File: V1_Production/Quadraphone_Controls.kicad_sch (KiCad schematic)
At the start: 20 parts, among them J1 Conn_01x10_Female, J10 Pitch_In, J11 Mix_Out, J12 Conn_02x04_Top_Bottom, J13 Conn_01x04_Male, J14 Conn_01x01_Male, J2 Conn_01x10_Female, J3 Conn_01x10_Female, J4 Conn_01x10_Female, J5 PWM_CV, J6 LFO_IN, J7 PWM_CV_In, J8 Synch_Signal_In, J9 Freq_Mod_In, SW1 Synch_Type, SW2 Output_Type

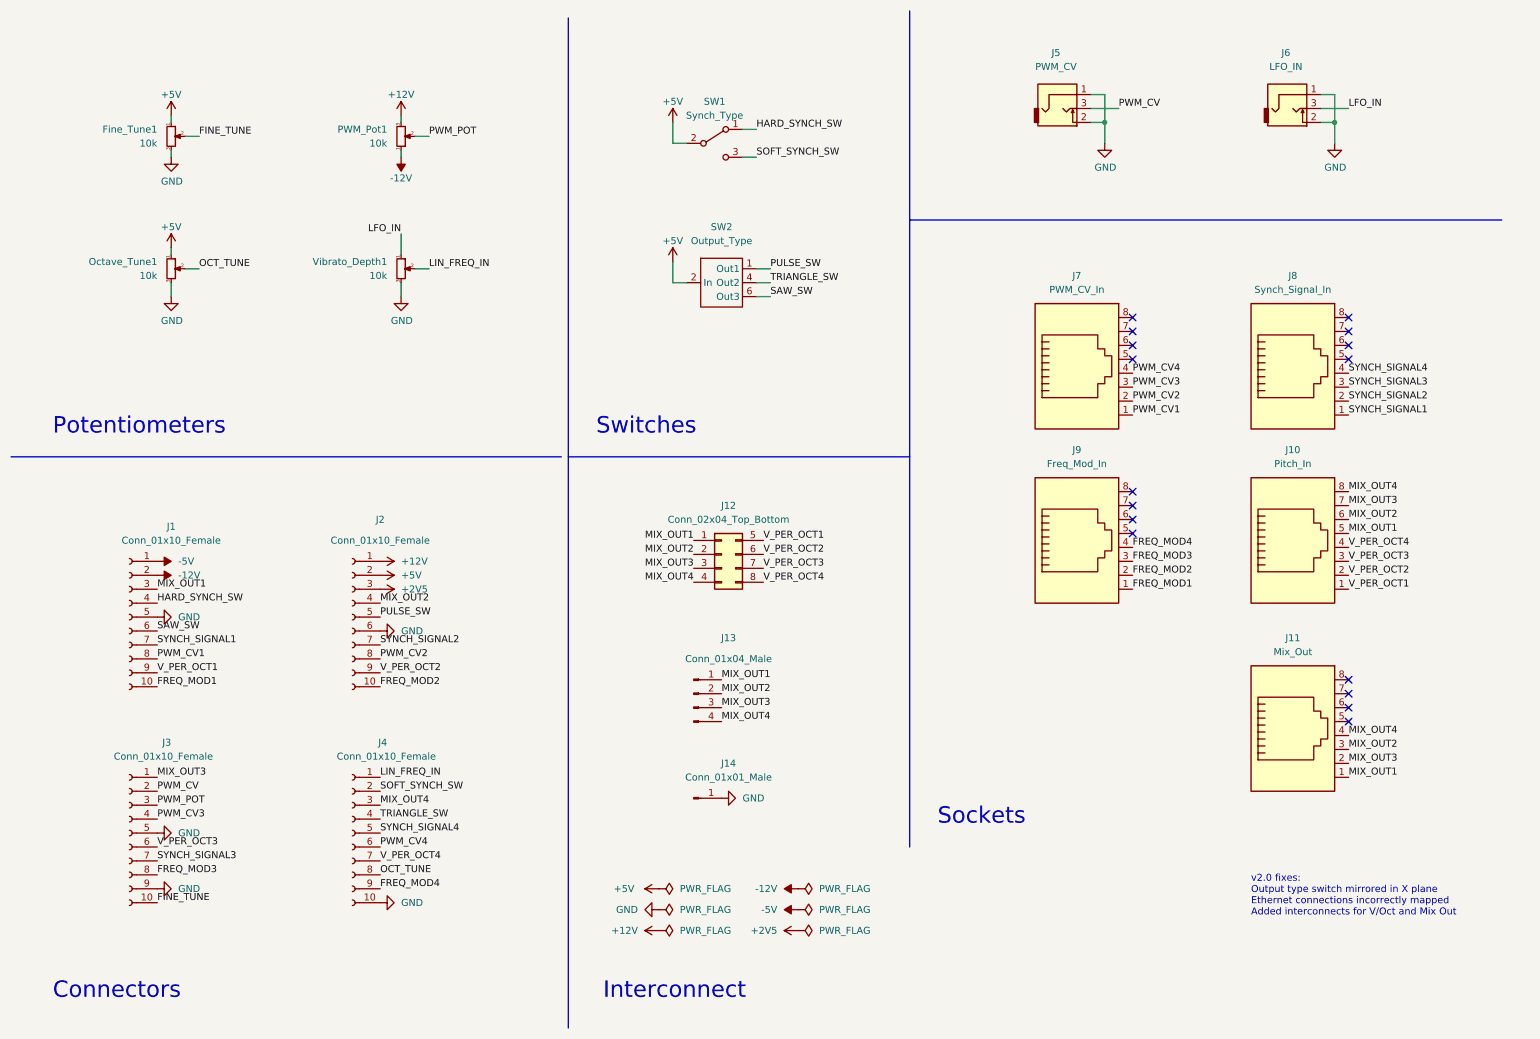
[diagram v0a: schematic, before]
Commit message: Updates for v2 on control board
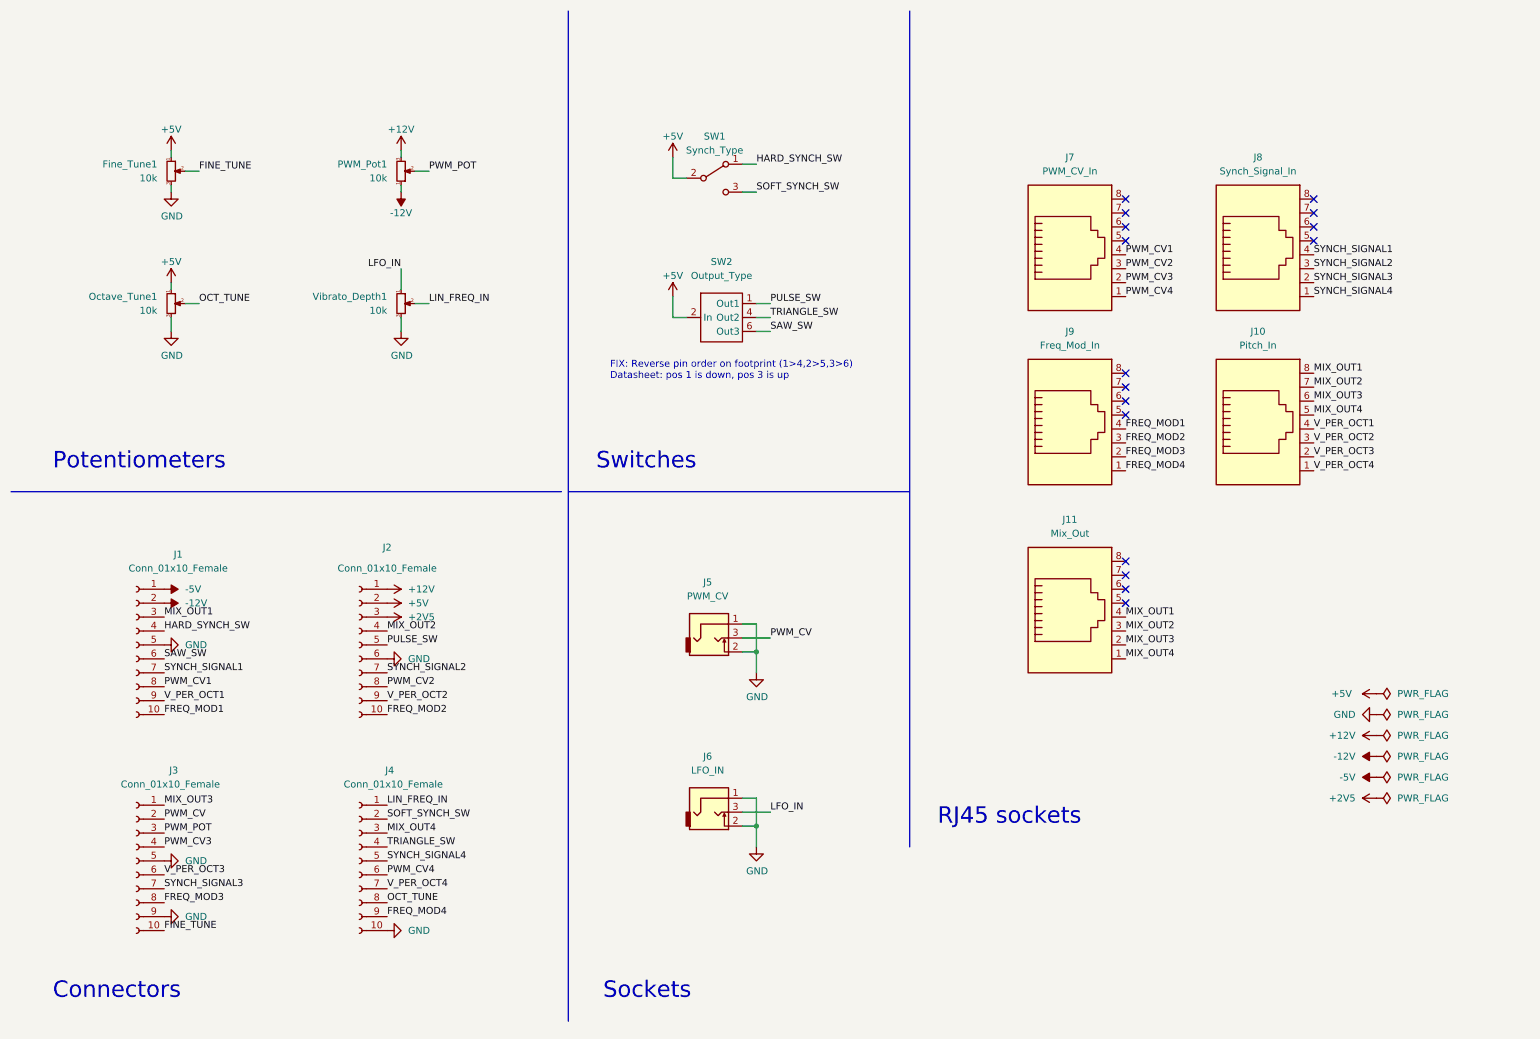
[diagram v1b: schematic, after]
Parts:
- removed J12: Conn_02x04_Top_Bottom, Connector_PinHeader_2.54mm:PinHeader_2x04_P2.54mm_Vertical, symbol Connector_Generic:Conn_02x04_Top_Bottom
- removed J13: Conn_01x04_Male, Connector_PinHeader_2.54mm:PinHeader_1x04_P2.54mm_Vertical, symbol Connector:Conn_01x04_Male
- removed J14: Conn_01x01_Male, Connector_PinHeader_2.54mm:PinHeader_1x01_P2.54mm_Vertical, symbol Connector:Conn_01x01_Male
- SW2: footprint Custom_Footprints:100DP6T1B1M2QE_ON_ON_ON -> Custom_Footprints:SW_100DP3T1B1M2QEH
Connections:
- net FREQ_MOD1: now also J9.4; no longer J9.1
- net FREQ_MOD2: now also J9.3; no longer J9.2
- net FREQ_MOD3: now also J9.2; no longer J9.3
- net FREQ_MOD4: now also J9.1; no longer J9.4
- net MIX_OUT1: now also J10.8, J11.4; no longer J10.5, J11.1
- net MIX_OUT2: now also J10.7; no longer J10.6
- net MIX_OUT3: now also J10.6; no longer J10.7
- net MIX_OUT4: now also J10.5, J11.1; no longer J10.8, J11.4
- net PWM_CV1: now also J7.4; no longer J7.1
- net PWM_CV2: now also J7.3; no longer J7.2
- net PWM_CV3: now also J7.2; no longer J7.3
- net PWM_CV4: now also J7.1; no longer J7.4
- net SYNCH_SIGNAL1: now also J8.4; no longer J8.1
- net SYNCH_SIGNAL2: now also J8.3; no longer J8.2
- net SYNCH_SIGNAL3: now also J8.2; no longer J8.3
- net SYNCH_SIGNAL4: now also J8.1; no longer J8.4
- net V_PER_OCT1: now also J10.4; no longer J10.1
- net V_PER_OCT2: now also J10.3; no longer J10.2
- net V_PER_OCT3: now also J10.2; no longer J10.3
- net V_PER_OCT4: now also J10.1; no longer J10.4
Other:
- note added: "FIX: Reverse pin order on footprint (1>4,2>5,3>6) Datasheet: pos 1 is down, pos 3 is up"
- note added: "RJ45 sockets"
- note removed: "Interconnect"
- note removed: "v2.0 fixes: Output type switch mirrored in X plane Ethernet connections incorrectly mapped Added interconnects for V/Oct and Mix Out"
- moved on the sheet: Fine_Tune1, J1, J10, J11, J2, J3, J4, J5, J6, J7, J8, J9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
